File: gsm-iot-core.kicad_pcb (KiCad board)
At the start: 2 copper layers, 25.4 x 61 mm, 93 parts, among them J1 MICRO_SD_HINGE - Micro SD soc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, P1 CONN_01X17, P2 CONN_01X17, P3 Chip anten, Q1 2SC1815, Q2 2SC1815, SW1 SW_PUSH, SW2 SW_PUSH, U1 MP2365DN, U2 LP2985-50DBVR, U3 STM32F405RGTx, U4 MMA7660, U5 SIM800C, U6 SIM HOLD - PPSS-6P, X1 CRYSTAL-24M, Y1 32.768MHz

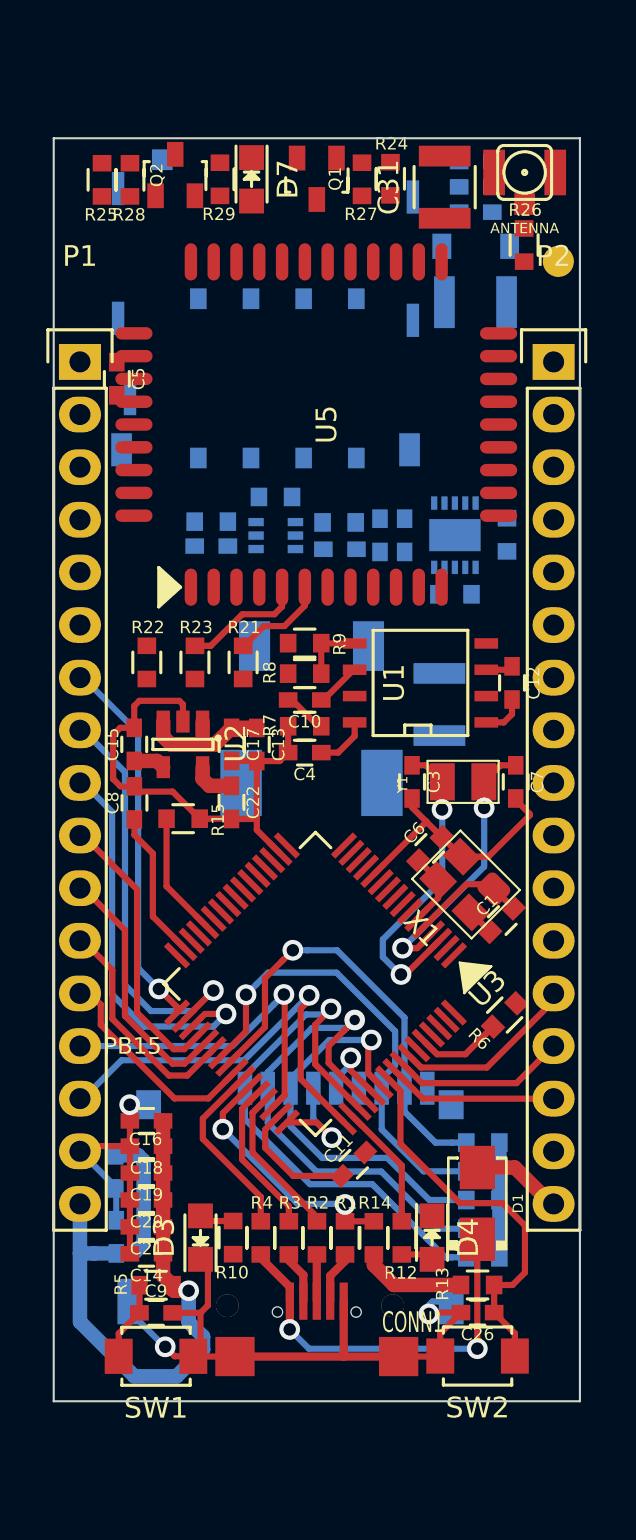
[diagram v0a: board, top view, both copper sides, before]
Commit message: all connect usb & SD card well
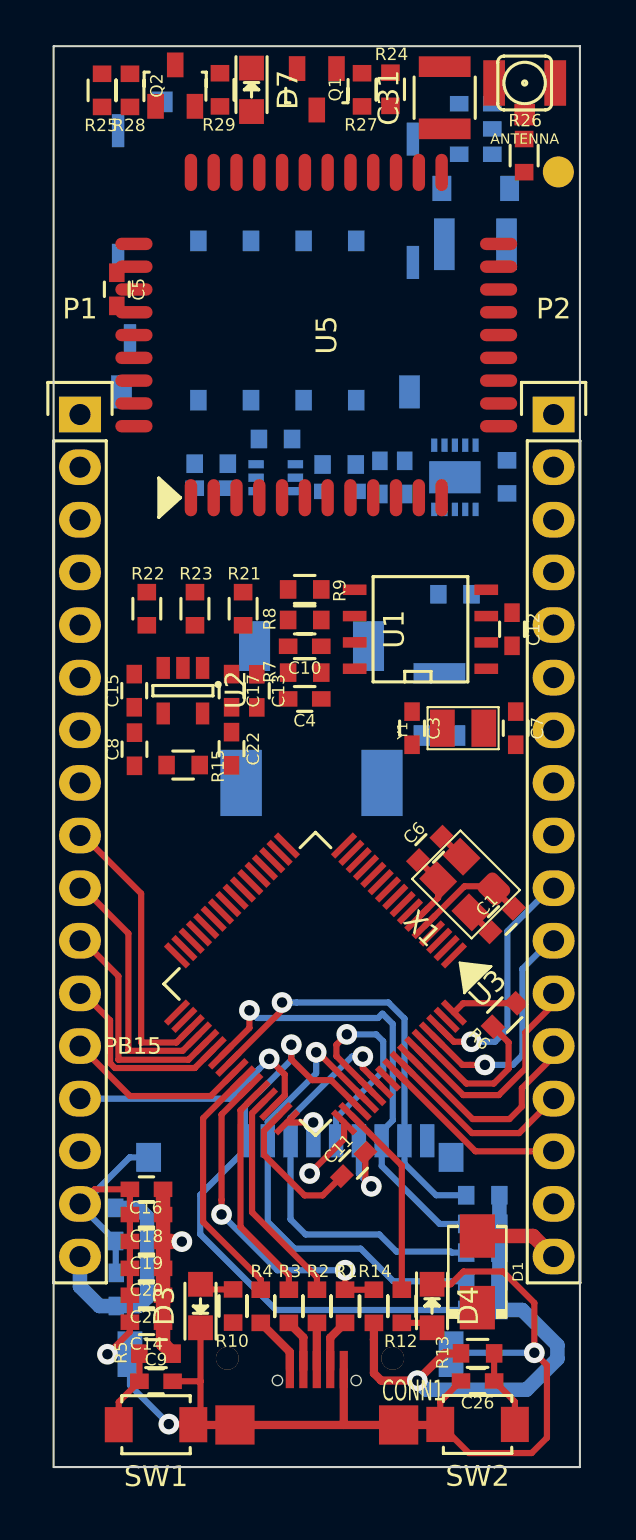
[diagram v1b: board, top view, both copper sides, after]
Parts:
- moved C31 4.32 mm to (167.5, 63.4)
- moved D7 4.32 mm to (158.1, 63.1)
- moved Q2 4.32 mm to (154.5, 62.9)
- moved R25 4.32 mm to (150.9, 63.1)
- moved R27 4.32 mm to (163.5, 63.1)
- moved R28 4.32 mm to (152.3, 63.1)
- moved R29 4.32 mm to (156.6, 63.1)
- moved ANT1 4.32 mm to (171.3, 62.7)
- moved C5 4.32 mm to (151.6, 72.7)
- moved P3 4.32 mm to (172.9, 67.0)
- moved Q1 4.32 mm to (161.3, 63.0)
- moved R24 4.32 mm to (164.8, 63.0)
- moved R26 4.32 mm to (171.3, 66.2)
- moved U5 4.32 mm to (161.3, 74.9)
- moved C16 3.30 mm to (153.1, 116.1)
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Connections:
- D5 pad 1: (no net) -> Net-(D5-Pad1)
- J1 pad 9: (no net) -> Net-(J1-Pad9)
- U1 pad 7: (no net) -> Net-(U1-Pad7)
- U4 pad 2: (no net) -> Net-(U4-Pad2)
- U5 pad 10: (no net) -> Net-(U5-Pad10)
- U5 pad 11: (no net) -> Net-(U5-Pad11)
- U5 pad 12: (no net) -> Net-(U5-Pad12)
- U5 pad 14: (no net) -> Net-(U5-Pad14)
- U5 pad 20: (no net) -> Net-(U5-Pad20)
- U5 pad 22: (no net) -> Net-(U5-Pad22)
- U5 pad 23: (no net) -> Net-(U5-Pad23)
- U5 pad 24: (no net) -> Net-(U5-Pad24)
- U5 pad 25: (no net) -> Net-(U5-Pad25)
- U5 pad 26: (no net) -> Net-(U5-Pad26)
- U5 pad 29: (no net) -> Net-(U5-Pad29)
- U5 pad 3: (no net) -> Net-(U5-Pad3)
- U5 pad 38: (no net) -> Net-(U5-Pad38)
- U5 pad 4: (no net) -> Net-(U5-Pad4)
- U5 pad 40: (no net) -> Net-(U5-Pad40)
- U5 pad 42: (no net) -> Net-(U5-Pad42)
- U5 pad 9: (no net) -> Net-(U5-Pad9)
- U6 pad 6: (no net) -> Net-(U6-Pad6)
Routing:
- net PB13: track 20.5 -> 0.15 mm, vias 1 -> 0
- net PB12: track 18.2 -> 0.00 mm, vias 1 -> 0
- net PA14_SWCLK: track 20.3 -> 3.15 mm
- net Net-(CONN1-Pad1): track 18.9 -> 2.83 mm, vias 2 -> 0
- net Net-(C3-Pad1): track 15.2 -> 0.00 mm, vias 2 -> 0
- net PB3_BUTTON: track 18.9 -> 3.84 mm
- net Net-(C7-Pad1): track 13.2 -> 0.00 mm, vias 2 -> 0
- net PB9: track 0.00 -> 11.7 mm, vias 0 -> 1
- net PB8: track 0.00 -> 11.4 mm, vias 0 -> 1
- net PB7: track 0.00 -> 10.9 mm
- net PC12_SDIO_CK: track 3.90 -> 11.4 mm
- net Net-(C8-Pad1): track 7.20 -> 0.00 mm
- net VDD: track 6.87 -> 0.00 mm
- net Net-(R15-Pad1): track 5.98 -> 0.00 mm
- net Net-(R23-Pad2): track 5.93 -> 0.00 mm
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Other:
- board size 25.4 x 61 mm -> 25.4 x 68.6 mm
- net class Default: via_drill 0.6 -> 0.5

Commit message: completed connect tracks
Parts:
- removed C5: 100nF, lib:C_0603
- C11, C14, C16, R15: moved to B.Cu
- R16: moved to F.Cu
- X1: footprint lib:Crystal_SMD_3225_4Pads -> lib:Crystal_SMD_5032_4Pads
- moved C2 33.0 mm to (171.1, 125.5), turned to 180 degrees
- moved C14 32.8 mm to (163.2, 91.4), turned to 90 degrees
- moved C12 30.6 mm to (166.0, 119.3), turned to 0 degrees
- moved C16 27.3 mm to (164.5, 91.4), turned to 90 degrees
- moved C13 27.1 mm to (156.7, 119.2), turned to 180 degrees
- moved R9 26.7 mm to (160.6, 113.9)
- moved U1 26.7 mm to (166.1, 115.8)
- moved C17 25.8 mm to (156.7, 117.9), turned to 180 degrees
- moved R7 25.2 mm to (160.6, 116.4)
- moved C4 25.2 mm to (160.6, 117.7)
- moved C10 25.2 mm to (160.6, 115.1)
- moved R8 24.1 mm to (165.6, 112.2), turned to 0 degrees
- moved U2 23.5 mm to (156.5, 115.5), turned to 180 degrees
- moved P3 22.9 mm to (150.4, 70.9)
- moved C15 21.6 mm to (156.7, 113.2), turned to 0 degrees
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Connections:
- D5 pad 1: Net-(D5-Pad1) -> (no net)
- J1 pad 9: Net-(J1-Pad9) -> (no net)
- U1 pad 7: Net-(U1-Pad7) -> (no net)
- U4 pad 2: Net-(U4-Pad2) -> (no net)
- U5 pad 10: Net-(U5-Pad10) -> (no net)
- U5 pad 11: Net-(U5-Pad11) -> (no net)
- U5 pad 12: Net-(U5-Pad12) -> (no net)
- U5 pad 14: Net-(U5-Pad14) -> (no net)
- U5 pad 20: Net-(U5-Pad20) -> (no net)
- U5 pad 22: Net-(U5-Pad22) -> (no net)
- U5 pad 23: Net-(U5-Pad23) -> (no net)
- U5 pad 24: Net-(U5-Pad24) -> (no net)
- U5 pad 25: Net-(U5-Pad25) -> (no net)
- U5 pad 26: Net-(U5-Pad26) -> (no net)
- U5 pad 29: Net-(U5-Pad29) -> (no net)
- U5 pad 3: Net-(U5-Pad3) -> (no net)
- U5 pad 38: Net-(U5-Pad38) -> (no net)
- U5 pad 4: Net-(U5-Pad4) -> (no net)
- U5 pad 40: Net-(U5-Pad40) -> (no net)
- U5 pad 42: Net-(U5-Pad42) -> (no net)
- U5 pad 9: Net-(U5-Pad9) -> (no net)
- U6 pad 6: Net-(U6-Pad6) -> (no net)
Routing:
- net GND: track 78.7 -> 376.7 mm, vias 4 -> 23
- net +3V3: track 51.5 -> 196.8 mm, vias 3 -> 15
- net VDD: track 0.00 -> 90.6 mm, vias 0 -> 5
- net PA7_PWRKEY: track 0.00 -> 49.5 mm, vias 0 -> 2
- net Net-(C12-Pad1): track 0.00 -> 43.3 mm, vias 0 -> 3
- net PA15_LED: track 9.44 -> 49.8 mm, vias 0 -> 2
- net /RST: track 3.84 -> 40.4 mm, vias 0 -> 2
- net Net-(D5-Pad3): track 0.00 -> 30.9 mm, vias 0 -> 2
- net PA1: track 0.00 -> 23.3 mm, vias 0 -> 2
- net SIM800C_PWRKEY: track 0.00 -> 23.2 mm, vias 0 -> 2
- net PB3_BUTTON: track 3.84 -> 24.5 mm, vias 0 -> 2
- net PC0: track 0.00 -> 20.0 mm, vias 0 -> 1
- net Net-(C7-Pad1): track 0.00 -> 19.9 mm, vias 0 -> 2
- net SIM800C_NETLIGHT: track 0.00 -> 19.0 mm, vias 0 -> 2
- net PC1: track 0.00 -> 18.8 mm, vias 0 -> 1
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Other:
- board size 25.4 x 68.6 mm -> 25.4 x 64.8 mm
- net class Default: clearance 0.1 -> 0.254
- rule trace_clearance: 0.1 -> 0.254

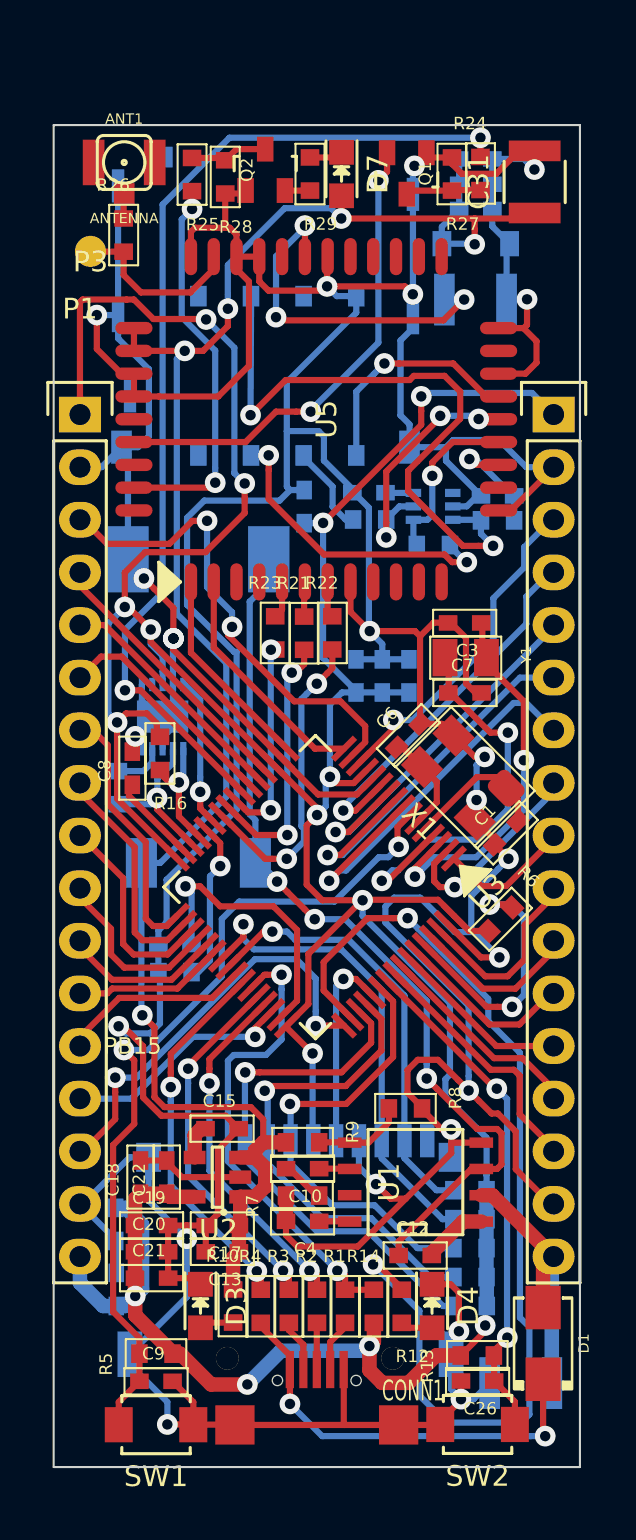
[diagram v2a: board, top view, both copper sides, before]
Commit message: fix 1/3 via & track distance
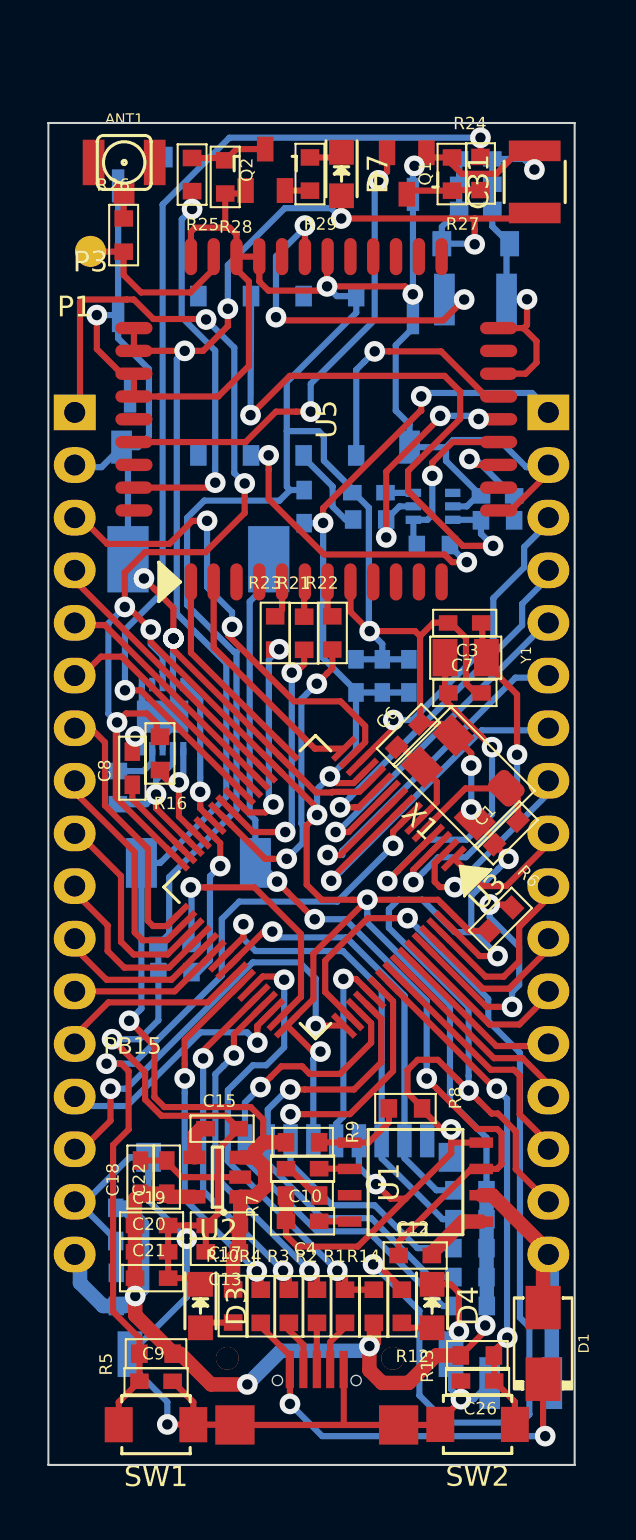
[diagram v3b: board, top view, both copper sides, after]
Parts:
- moved P1 0.27 mm to (149.6, 78.6)
- moved P2 0.27 mm to (172.5, 78.6)
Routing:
- net Net-(C7-Pad1): track 19.9 -> 17.9 mm
- net GND: track 376.7 -> 375.1 mm
- net PC0: track 20.0 -> 18.7 mm
- net SIM800C_VDD: track 11.2 -> 12.3 mm
- net PA13_SWDIO: track 11.3 -> 12.2 mm
- net Net-(R6-Pad2): track 13.1 -> 12.3 mm
- net /RST: track 40.4 -> 41.2 mm
- net PA11_DM: track 17.6 -> 17.0 mm
- net PA10_ID: track 22.8 -> 22.2 mm
- net PA9_VBUS: track 18.1 -> 17.6 mm
- net PC10_SDIO_D2: track 26.2 -> 25.6 mm
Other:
- net class Default: clearance 0.254 -> 0.1
- rule trace_clearance: 0.254 -> 0.1

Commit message: Final pcb
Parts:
- moved P1 0.10 mm to (149.6, 78.7)
- moved P2 0.10 mm to (172.5, 78.7)
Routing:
- net +3V3: track 196.9 -> 199.4 mm
- net Net-(D5-Pad3): track 30.9 -> 29.0 mm
- net VDD: track 91.1 -> 92.8 mm
- net Net-(R19-Pad1): track 15.0 -> 16.5 mm
- net SIM800C_DATA: track 5.65 -> 4.50 mm
- net SIM800C_RI: track 15.1 -> 16.0 mm
- net GND: track 375.1 -> 374.2 mm, vias 23 -> 22
- net PA15_LED: track 49.7 -> 49.0 mm
- net GSM_ANT: track 8.50 -> 7.79 mm
- net Net-(R6-Pad2): track 12.3 -> 11.7 mm
- net PA6: track 11.2 -> 10.7 mm
- net PA10_ID: track 22.2 -> 21.7 mm
- added copper zone on B.Cu, net GND
- added copper zone on F.Cu, net GND
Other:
- board text added: "3.3V"
- board text added: "5V"
- board text added: "GND"
- board text added: "PA0"
- board text added: "PA1"
- board text added: "PA4"
- board text added: "PA5"
- board text added: "PA6"
- board text added: "PA8"
- board text added: "PB12"
- board text added: "PB13"
- board text added: "PB14"
- board text added: "PB4"
- board text added: "PB5"
- board text added: "PB6"
- board text added: "PB7"
- board text added: "PB8"
- board text added: "PB9"
- board text added: "PC0"
- board text added: "PC1"
- board text added: "PC13"
- board text added: "PC2"
- board text added: "PC3"
- board text added: "PC6"
- board text added: "PC7"
- board text added: "SWCLK"
- board text added: "SWDIO"
- board text added: "VBAT"
